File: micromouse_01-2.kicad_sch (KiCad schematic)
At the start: 64 parts, among them IC6 PCA9632TK,118, J1 Conn_01x02_Pin, M3 Fan_Motor, Q1 MCM3400A-TP, Q2 MCM3400A-TP, Q3 MCM3400A-TP, Q4 Q_PMOS_GSD, Q5 Q_PMOS_GSD, Q6 Q_PMOS_GSD, SW3 SSSS810701, U1 SMT-0440-S-R, U2 LBR-127HLD, U3 LBR-127HLD, U4 LBR-127HLD, U5 LBR-127HLD, U6 LXDC55FAAA-203, U7 MCP73831-2-OT, U8 WS2812-2020

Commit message: [update]けっこう線引いた
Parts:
- removed D12: 1N4148W, Diode_SMD:D_SOD-123, symbol Diode:1N4148W
- removed D7: 1N5819HW-7-F, footprints:SOD3715X145N, symbol 1N5819HW-7-F:1N5819HW-7-F
- removed M3: Fan_Motor, footprints:MK06-4.5, symbol Motor:Motor_DC
- added D5, D7: CCS15S40,L3F, footprints:SOD-963 CST2C_TOS, symbol Diode:1N4148W
- added J2: Fan+, footprints:Pad_1, symbol Connector_Generic:Conn_01x01
- added J4: Fan-, footprints:Pad_1, symbol Connector_Generic:Conn_01x01
- J1: footprint footprints:power_SMD -> footprints:MK06-4.5
- Q1, Q2, Q3: footprint footprints:DFN2020-6L_MCE -> DFN2020-6L_MCE
- renumbered C13 to C10, C10 to C11, C12 to C2, C12 to C8, D1 to D2, R16 to R10, R10 to R11, R17 to R12, R11 to R13, R18 to R14, R19 to R15, R1 to R16, R22 to R17, R17 to R22, R1 to R25, R1 to R26, R1 to R30, R1 to R31, R12 to R4, R8 to R5, R13 to R6, R9 to R7, R14 to R8, R15 to R9
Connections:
- net +BATT: now also J2.1 (Pin_1)
- net GND: now also SW3.2 (B); no longer SW3.1 (A)
- net VBUS: now also D5.2 (A), D7.2 (A)
- net at D2.2 (A), Q3.3: now also J4.1 (Pin_1)
- net at Q6.1 (G), R27.2: now also SW3.1 (A); no longer SW3.2 (B)
- net at Q5.2 (S), Q6.2 (S), R27.1: now also D7.1 (K)
- net at Q4.1 (G), Q5.1 (G), R24.1: now also D5.1 (K)
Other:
- moved on the sheet: C10, C11, C13, C17, C18, C19, C2, C8, D1, D10, D2, D3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

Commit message: [add]3Dモデル追加
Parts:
- R25, R26, R30, R31: value 1k -> 2.4k
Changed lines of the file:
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@@
       (effects (font (size 1.27 1.27)) (justify left))
     )
-    (property "Value" "1k" (at 196.85 29.21 0)
+    (property "Value" "2.4k" (at 196.85 29.21 0)
       (effects (font (size 1.27 1.27)) (justify left))
     )
@@
       (effects (font (size 1.27 1.27)) (justify left))
     )
-    (property "Value" "1k" (at 187.96 29.21 0)
+    (property "Value" "2.4k" (at 187.96 29.21 0)
       (effects (font (size 1.27 1.27)) (justify left))
     )
@@
       (effects (font (size 1.27 1.27)) (justify left))
     )
-    (property "Value" "1k" (at 179.07 29.21 0)
+    (property "Value" "2.4k" (at 179.07 29.21 0)
       (effects (font (size 1.27 1.27)) (justify left))
     )
@@
       (effects (font (size 1.27 1.27)) (justify left))
     )
-    (property "Value" "1k" (at 170.18 29.21 0)
-      (effects (font (size 1.27 1.27)) (justify left))
-    )
+    (property "Value" "2.4k" (at 170.18 29.21 0)
+      (effects (font (size 1.27 1.27)) (justify left))
+    )

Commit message: PICO-1-N8R2用回路
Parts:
- C18, C19: footprint Capacitor_SMD:C_0402_1005Metric -> Capacitor_SMD:C_0603_1608Metric
- R24, R27: value R -> 1k
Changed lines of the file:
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@@
       (effects (font (size 1.27 1.27)) (justify right))
     )
-    (property "Footprint" "Capacitor_SMD:C_0402_1005Metric" (at 155.2448 143.51 0)
+    (property "Footprint" "Capacitor_SMD:C_0603_1608Metric" (at 155.2448 143.51 0)
       (effects (font (size 1.27 1.27)) hide)
     )
@@
       (effects (font (size 1.27 1.27)) (justify left))
     )
-    (property "Value" "R" (at 234.95 128.27 0)
+    (property "Value" "1k" (at 234.95 128.27 0)
       (effects (font (size 1.27 1.27)) (justify left))
     )
@@
       (effects (font (size 1.27 1.27)) (justify left))
     )
-    (property "Value" "R" (at 212.09 146.05 0)
+    (property "Value" "1k" (at 212.09 146.05 0)
       (effects (font (size 1.27 1.27)) (justify left))
     )
@@
       (effects (font (size 1.27 1.27)) (justify right))
     )
-    (property "Footprint" "Capacitor_SMD:C_0402_1005Metric" (at 150.1648 123.19 0)
-      (effects (font (size 1.27 1.27)) hide)
-    )
+    (property "Footprint" "Capacitor_SMD:C_0603_1608Metric" (at 150.1648 123.19 0)
+      (effects (font (size 1.27 1.27)) hide)
+    )

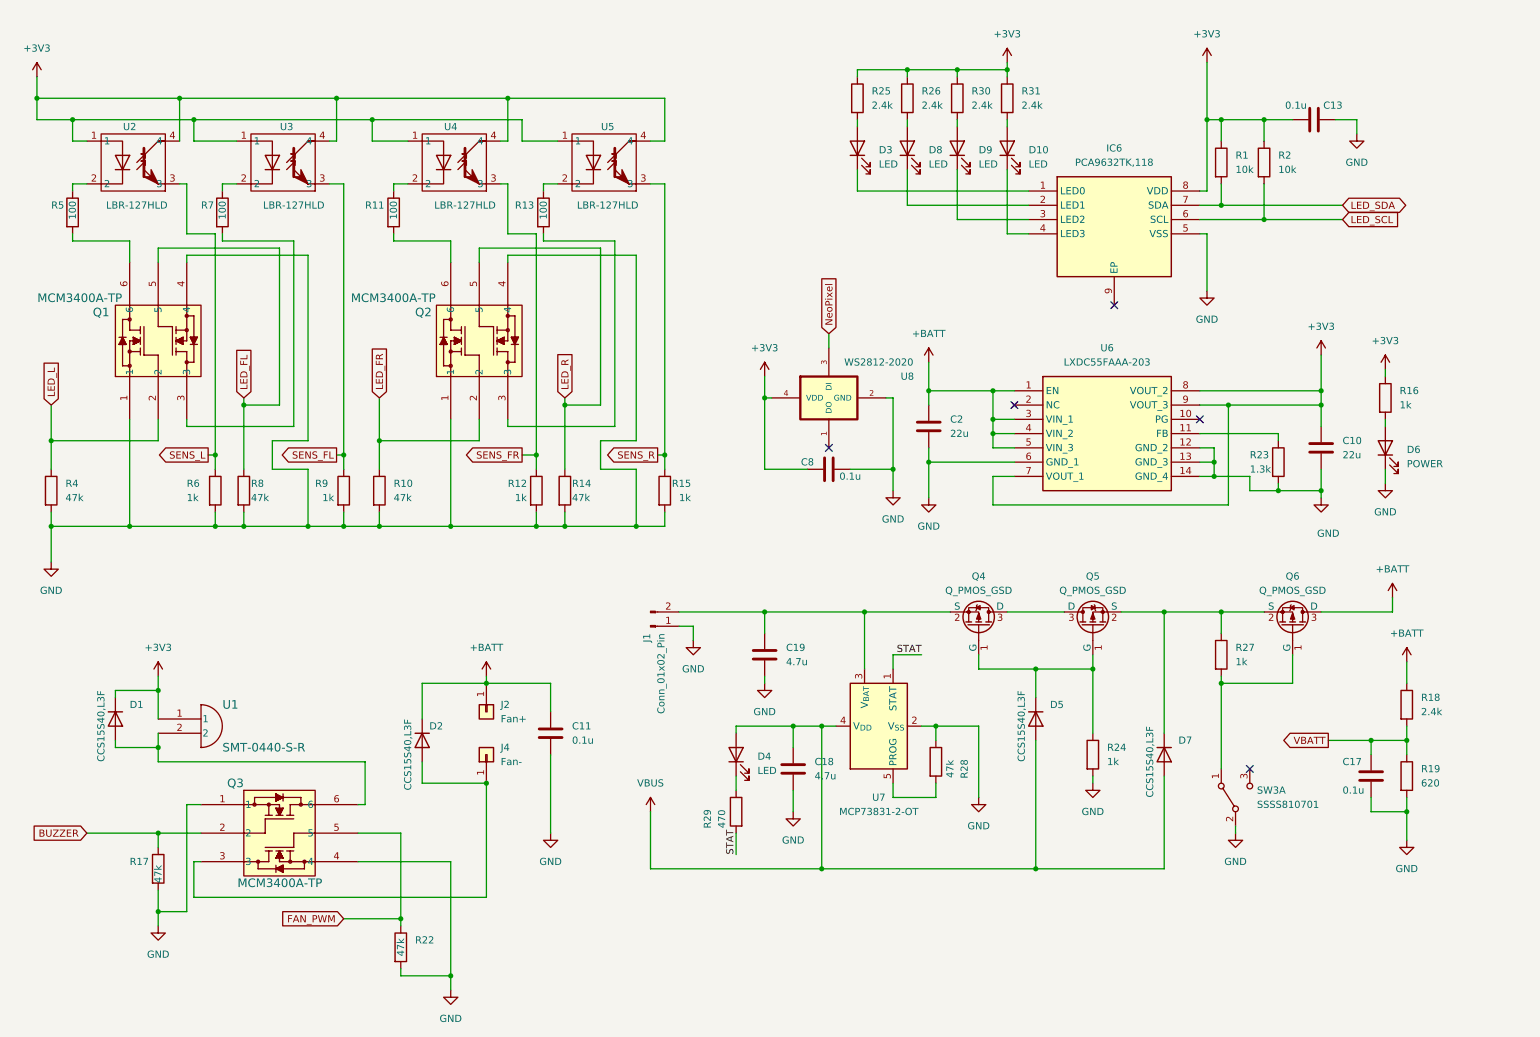
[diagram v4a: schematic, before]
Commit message: [update]ADCと壁センサ周りを変更
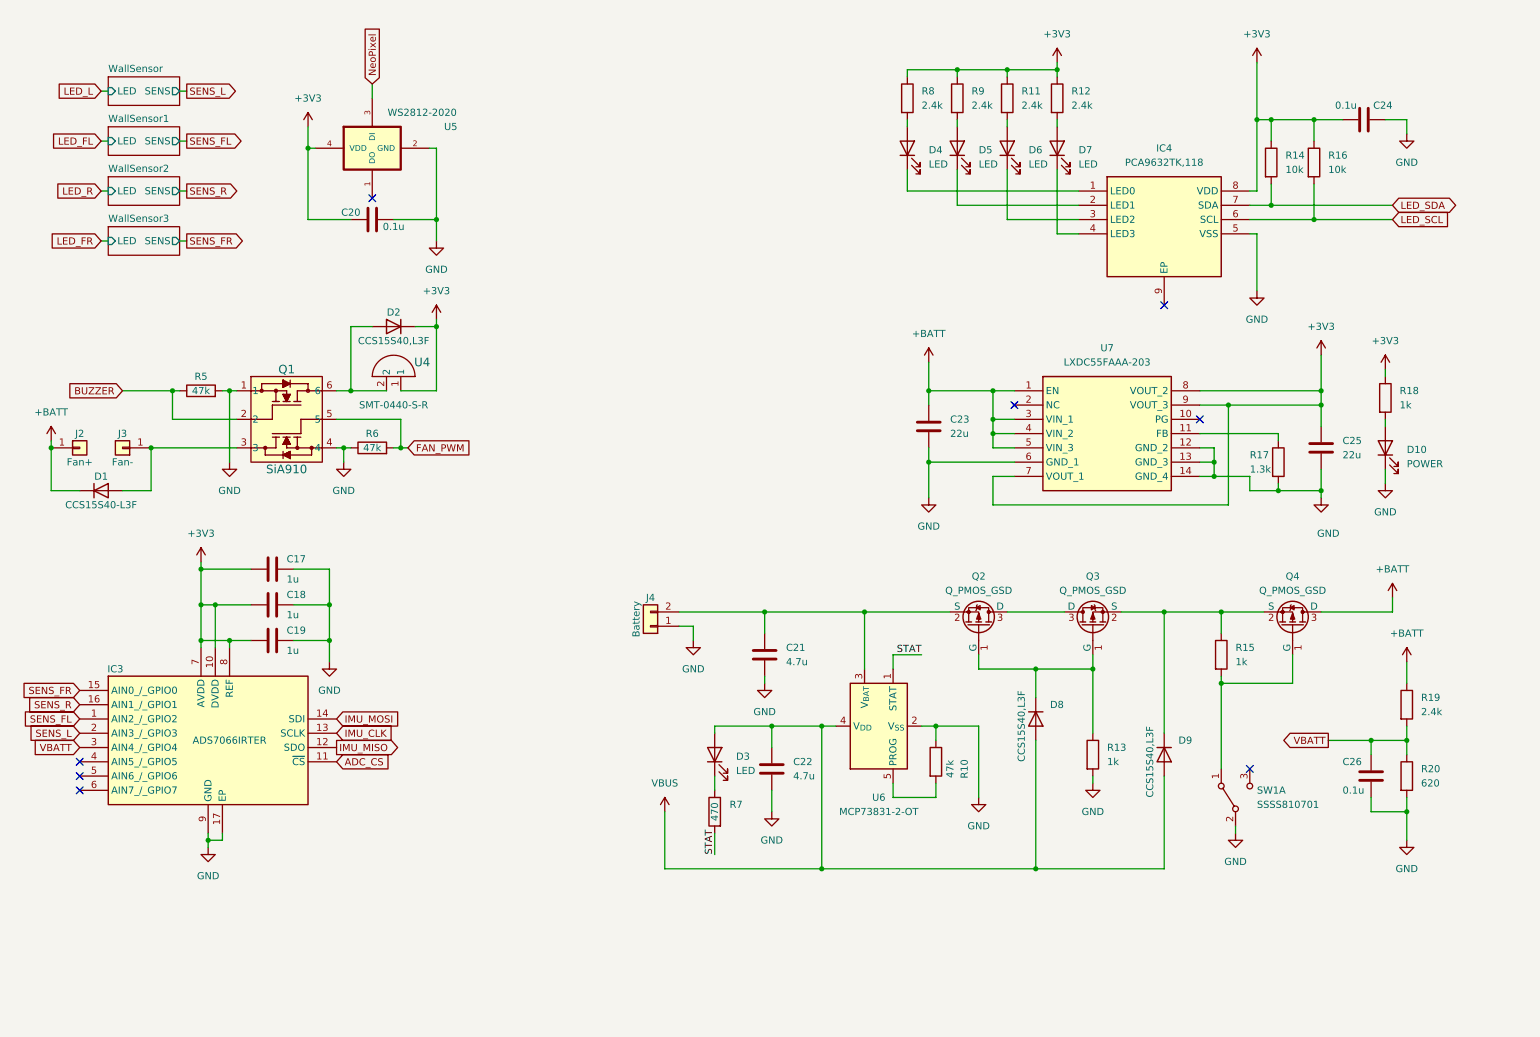
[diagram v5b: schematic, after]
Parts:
- removed C11: 0.1u, Capacitor_SMD:C_0402_1005Metric, symbol Device:C
- removed J1: Conn_01x02_Pin, footprints:MK06-4.5, symbol Connector:Conn_01x02_Pin
- removed Q1, Q2, Q3: MCM3400A-TP, DFN2020-6L_MCE, symbol MCM3400A-TP:MCM3400A-TP
- removed R10, R14, R22, R4, R8: 47k, Resistor_SMD:R_0402_1005Metric, symbol Device:R
- removed R11, R13, R5, R7: 100, Resistor_SMD:R_0402_1005Metric, symbol Device:R
- removed R12, R15, R9: 1k, Resistor_SMD:R_0402_1005Metric, symbol Device:R
- removed U2, U3, U4, U5: LBR-127HLD, footprints:LBR-127HLD, symbol New_Library:LBR-127HLD
- added C17, C18, C19: 1u, Capacitor_SMD:C_0402_1005Metric, symbol Device:C
- added IC3: ADS7066IRTER, QFN50P300X300X80-17N-D, symbol ADS7066IRTER:ADS7066IRTER
- added J4: Battery, symbol Connector_Generic:Conn_01x02
- added Q1: SiA910, Package_TO_SOT_SMD:Vishay_PowerPAK_SC70-6L_Dual, symbol SiA910:SiA910EDJ
- D1: renamed from D2; value CCS15S40,L3F -> CCS15S40-L3F
- R5: renamed from R17; value 47k -> 47k
- R6: value 1k -> 47k
- U4: renamed from U1; footprint footprints:SMT-0440-S-R_PUI -> SMT-0440-S-R_PUI
- renumbered C8 to C20, C19 to C21, C18 to C22, C2 to C23, C13 to C24, C10 to C25, C17 to C26, D6 to D10, D1 to D2, D4 to D3, D3 to D4, D8 to D5, D9 to D6, D10 to D7, D5 to D8, D7 to D9, IC6 to IC4, J4 to J3, Q4 to Q2, Q5 to Q3, Q6 to Q4, R28 to R10, R30 to R11, R31 to R12, R24 to R13, R1 to R14, R27 to R15, R2 to R16, R23 to R17, R16 to R18, R18 to R19, R19 to R20, R29 to R7, R25 to R8, R26 to R9, SW3 to SW1, U8 to U5, U7 to U6, U6 to U7
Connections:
- net +3V3: now also C17.1, C18.1, C19.1, IC3.10 (DVDD), IC3.7 (AVDD), IC3.8 (REF)
- net BUZZER: now also Q1.2
- net FAN_PWM: now also R6.2, Q1.5
- net GND: now also R6.1, C17.2, C18.2, C19.2, IC3.17 (EP), IC3.9 (GND), J4.1 (Pin_1), Q1.1, Q1.4; no longer R6.2
- net SENS_FL: now also IC3.1 (AIN2_/_GPIO2)
- net SENS_FR: now also IC3.15 (AIN0_/_GPIO0)
- net SENS_L: now also IC3.2 (AIN3_/_GPIO3); no longer R6.1
- net SENS_R: now also IC3.16 (AIN1_/_GPIO1)
- net VBATT: now also IC3.3 (AIN4_/_GPIO4)
- net at D1.2 (A), J3.1 (Pin_1): now also Q1.3
- net at D2.2 (A), U4.2: now also Q1.6
- net at C21.2, Q2.2 (S), U6.3 (V_{BAT}): now also J4.2 (Pin_2)
- new net ADC_CS: IC3.11 (~{CS})
- new net IMU_CLK: IC3.13 (SCLK)
- new net IMU_MISO: IC3.12 (SDO)
- new net IMU_MOSI: IC3.14 (SDI)
- no-connect marks 5 -> 8
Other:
- added sheet WallSensor (WallSensor.kicad_sch)
- added sheet WallSensor1 (WallSensor.kicad_sch)
- added sheet WallSensor2 (WallSensor.kicad_sch)
- added sheet WallSensor3 (WallSensor.kicad_sch)
- moved on the sheet: C20, C22, C24, D1, D2, D3, D4, D5, D6, D7, IC4, J2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

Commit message: 新しい部品乗せた
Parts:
- J4: footprint (none) -> footprints:MK06-4.5
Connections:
- net SENS_FL: now also IC3.5 (AIN6_/_GPIO6); no longer IC3.1 (AIN2_/_GPIO2)
- net SENS_L: now also IC3.6 (AIN7_/_GPIO7); no longer IC3.2 (AIN3_/_GPIO3)
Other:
- moved on the sheet: C17, C18, C19, IC3

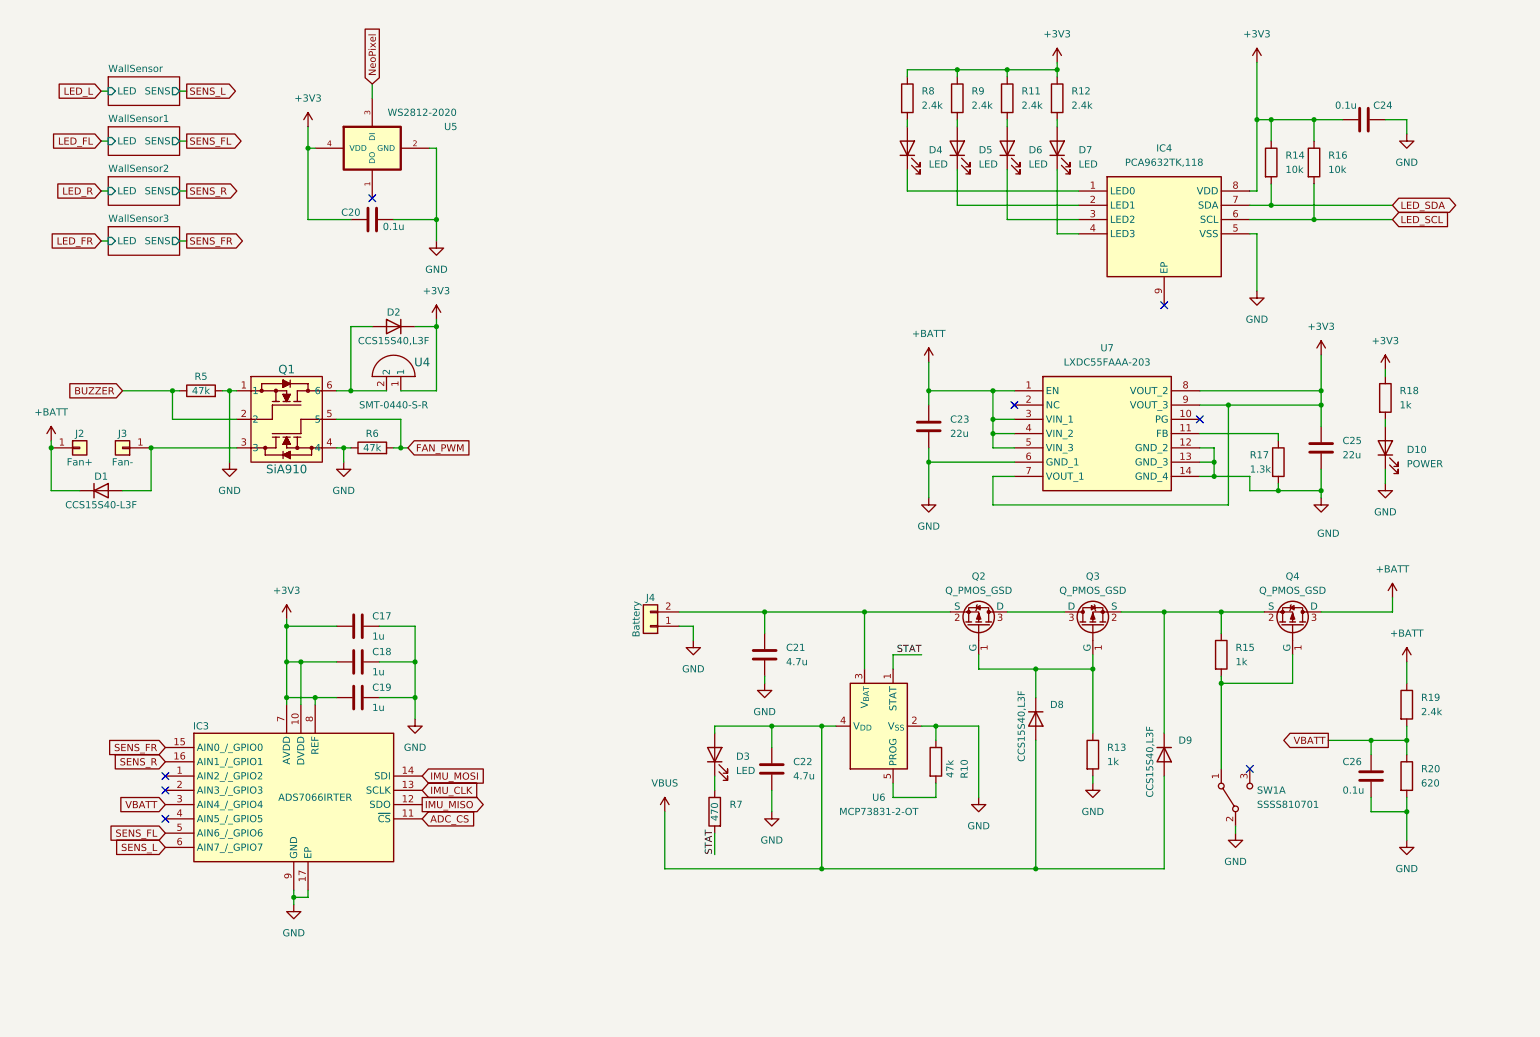
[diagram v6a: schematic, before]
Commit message: 回路図完成 PCB配線途中
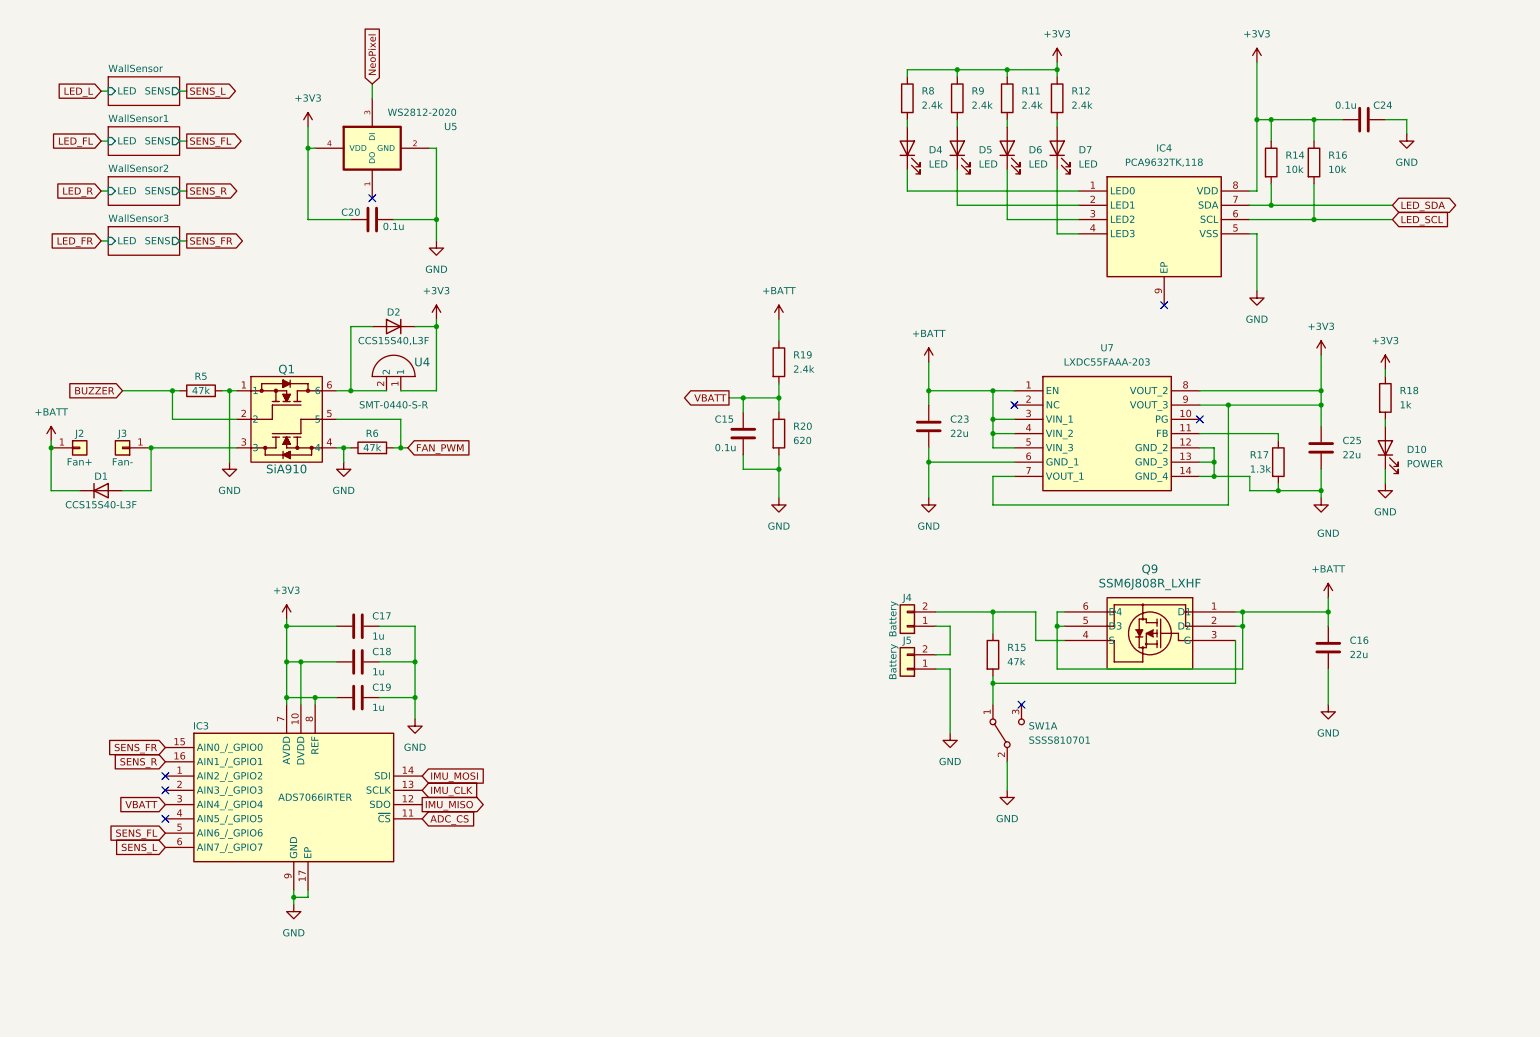
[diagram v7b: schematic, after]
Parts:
- removed C21, C22: 4.7u, Capacitor_SMD:C_0603_1608Metric, symbol Device:C
- removed C26: 0.1u, Capacitor_SMD:C_0402_1005Metric, symbol Device:C
- removed D3: LED, LED_SMD:LED_0402_1005Metric, symbol Device:LED
- removed D8, D9: CCS15S40,L3F, footprints:SOD-963 CST2C_TOS, symbol Diode:1N4148W
- removed Q2, Q3, Q4: Q_PMOS_GSD, Package_TO_SOT_SMD:SOT-23, symbol Device:Q_PMOS_GSD
- removed R10: 47k, Resistor_SMD:R_0402_1005Metric, symbol Device:R
- removed R13: 1k, Resistor_SMD:R_0402_1005Metric, symbol Device:R
- removed R7: 470, Resistor_SMD:R_0402_1005Metric, symbol Device:R
- removed U6: MCP73831-2-OT, Package_TO_SOT_SMD:SOT-23-5, symbol Battery_Management:MCP73831-2-OT
- added C15: 0.1u, Capacitor_SMD:C_0402_1005Metric, symbol Device:C
- added C16: 22u, Capacitor_SMD:C_0603_1608Metric, symbol Device:C
- added J5: Battery, footprints:CONN_B2B-ZRLFSN_JST, symbol Connector_Generic:Conn_01x02
- added Q9: SSM6J808R_LXHF, TSOP6F_SSM6J_TOS, symbol 2023-09-15_04-32-54:SSM6J808R_LXHF
- J4: footprint footprints:MK06-4.5 -> footprints:CONN_B2B-ZRLFSN_JST
- R15: value 1k -> 47k
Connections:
- net +BATT: now also C16.1, Q9.1 (D1), Q9.2 (D2), Q9.5 (D3), Q9.6 (D4)
- net GND: now also C15.2, C16.2, J5.1 (Pin_1); no longer J4.1 (Pin_1)
- net VBATT: now also C15.1
- net at R15.2, SW1.1 (A): now also Q9.3 (G)
- net at R15.1: now also J4.2 (Pin_2), Q9.4 (S)
- new net: J4.1 (Pin_1), J5.2 (Pin_2)
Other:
- moved on the sheet: J4, R15, SW1A
